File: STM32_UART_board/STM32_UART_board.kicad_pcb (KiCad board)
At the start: 2 copper layers, 30 parts, among them J1 SWD, J2 Scooter, Q1 AO4612_C4748739, SW1 SW_Push, SW2 SW_Push, U1 BAS70-05, U2 LM2574HVM-5, U3 AZ1117-3.3, U4 STM32C011F6Px

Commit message: almost done
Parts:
- R5, R6: moved to B.Cu
- moved H3 190.8 mm to (67.0, 46.0)
- moved C6 190.2 mm to (79.5, 72.0), turned to 90 degrees
- moved C5 185.5 mm to (81.5, 72.0), turned to 90 degrees
- moved C4 176.3 mm to (89.8, 75.0), turned to 0 degrees
- moved U3 175.3 mm to (86.2, 69.5), turned to 90 degrees
- moved C3 171.3 mm to (97.2, 78.0), turned to 0 degrees
- moved H1 168.9 mm to (67.0, 81.0)
- moved H4 163.4 mm to (107.5, 46.0)
- moved C1 160.6 mm to (86.2, 50.8), turned to -90 degrees
- moved L1 159.9 mm to (97.8, 66.5), turned to 180 degrees
- moved D1 148.8 mm to (100.2, 57.0), turned to 0 degrees
- moved U2 146.3 mm to (97.2, 49.5), turned to 180 degrees
- moved R4 135.6 mm to (79.5, 63.0), turned to -90 degrees
- moved H2 134.3 mm to (107.5, 81.0)
- moved J1 128.7 mm to (75.5, 78.5), turned to 90 degrees
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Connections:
- J1 pad 5: /3V3 -> +3.3V
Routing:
- net +3.3V: track 11.6 -> 60.7 mm, vias 0 -> 1
- net /PA13: track 0.00 -> 34.1 mm, vias 0 -> 1
- net /NRST: track 0.00 -> 29.6 mm, vias 0 -> 1
- net /PA14: track 0.00 -> 24.2 mm, vias 0 -> 1
- net /EN: track 0.00 -> 21.2 mm, vias 0 -> 1
- net /PA1: track 0.00 -> 21.1 mm
- net /BUTTON: track 3.11 -> 20.9 mm, vias 0 -> 1
- net /ON: track 2.15 -> 19.7 mm, vias 1 -> 2
- net /PA8: track 0.00 -> 11.4 mm
- net BATT+: track 10.8 -> 20.6 mm
- net /PC14: track 0.00 -> 7.77 mm
- net +36V: track 6.67 -> 12.1 mm
- net /Q1_G1: track 6.17 -> 10.2 mm
- net Net-(D2-A): track 0.00 -> 1.81 mm
- net GND: track 6.50 -> 4.98 mm, vias 0 -> 120
- added copper zone on B.Cu, net GND
- added copper zone on F.Cu, net GND
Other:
- board outline added: 47.5 x 42 mm

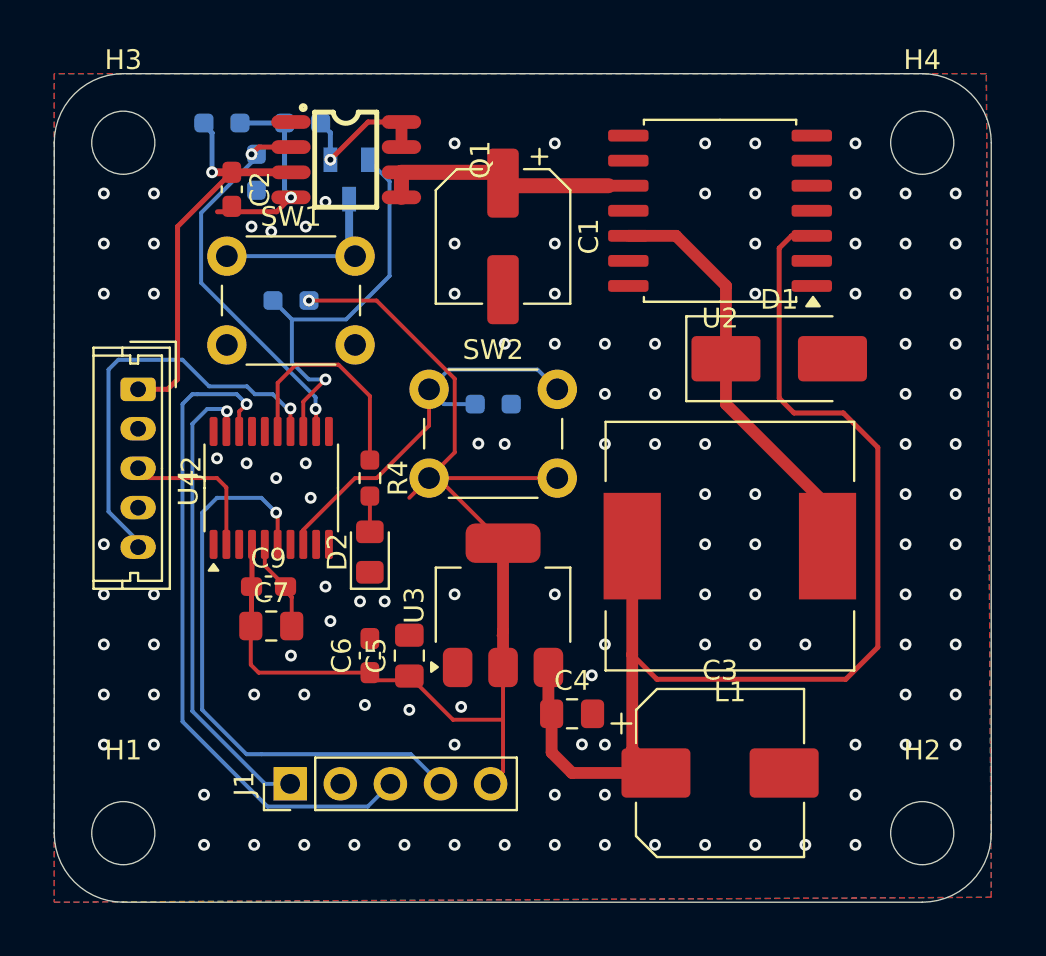
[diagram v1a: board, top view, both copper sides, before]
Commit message: added testpoints to the remaining pins
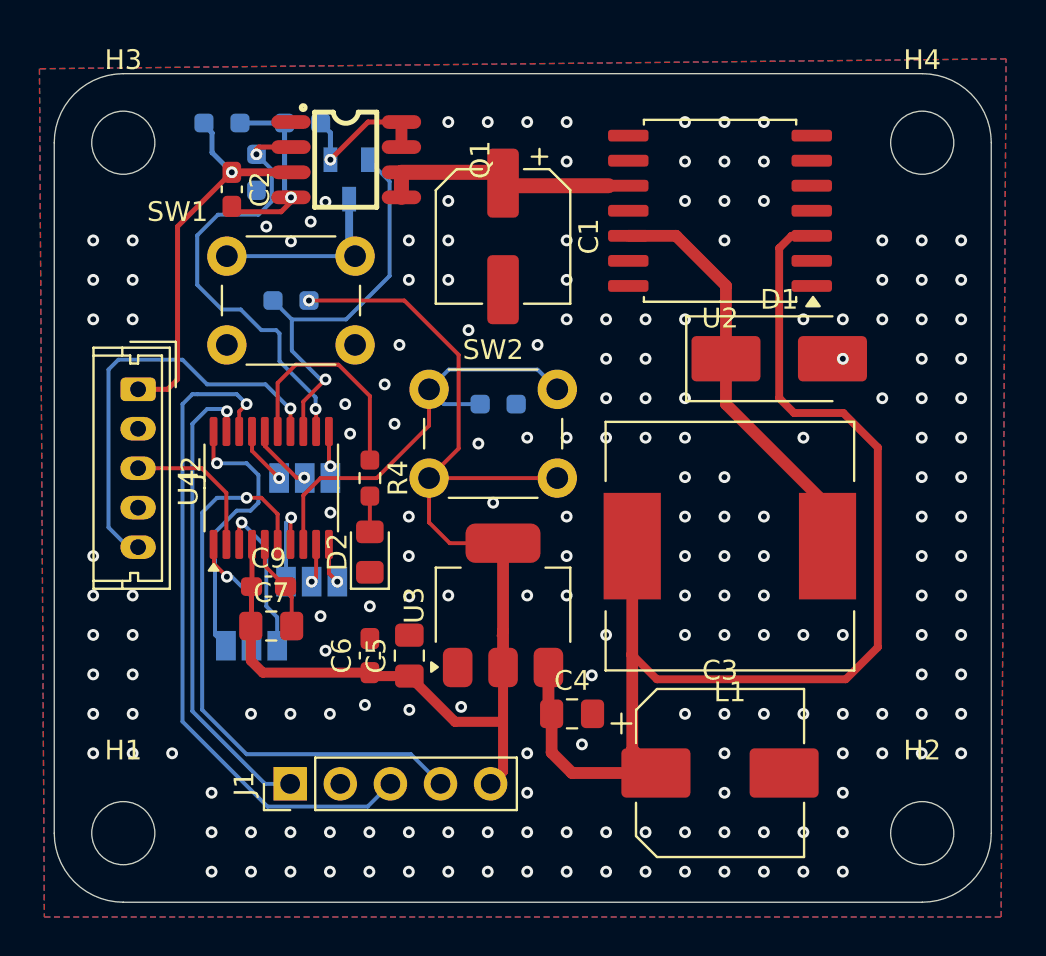
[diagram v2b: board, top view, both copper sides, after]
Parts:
- added JP1: SolderJumper_3_Open, Jumper:SolderJumper-3_P1.3mm_Open_Pad1.0x1.5mm, B.Cu at (76.5, 68.2)
- added JP2: SolderJumper_3_Open, Jumper:SolderJumper-3_P1.3mm_Open_Pad1.0x1.5mm, B.Cu at (76.2, 63.0)
- added JP3: SolderJumper_3_Open, Jumper:SolderJumper-3_P1.3mm_Open_Pad1.0x1.5mm, B.Cu at (73.5, 71.5)
- moved R6 0.25 mm to (86.0, 59.2)
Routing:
- net /PB6: track 0.00 -> 14.2 mm, vias 0 -> 1
- net /PC15: track 0.00 -> 8.16 mm, vias 0 -> 1
- net /PB7: track 0.00 -> 6.08 mm, vias 0 -> 1
- net +3.3V: track 60.7 -> 66.6 mm
- net /PA0: track 0.00 -> 4.73 mm, vias 0 -> 1
- net /BOOT0_USART1_TX: track 0.00 -> 3.40 mm, vias 0 -> 1
- net /ON: track 19.7 -> 22.7 mm
- net /BOOT0_USART1_RX: track 0.00 -> 2.93 mm, vias 0 -> 1
- net /PA3: track 0.00 -> 2.06 mm, vias 0 -> 1
- net /PA2: track 0.00 -> 1.98 mm, vias 0 -> 1
- net /PA4: track 0.00 -> 1.79 mm, vias 0 -> 1
- net /PA1: track 21.1 -> 22.1 mm
- net BATT+: track 20.6 -> 20.1 mm
- net GND: vias 120 -> 188
